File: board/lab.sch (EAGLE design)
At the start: 7 parts

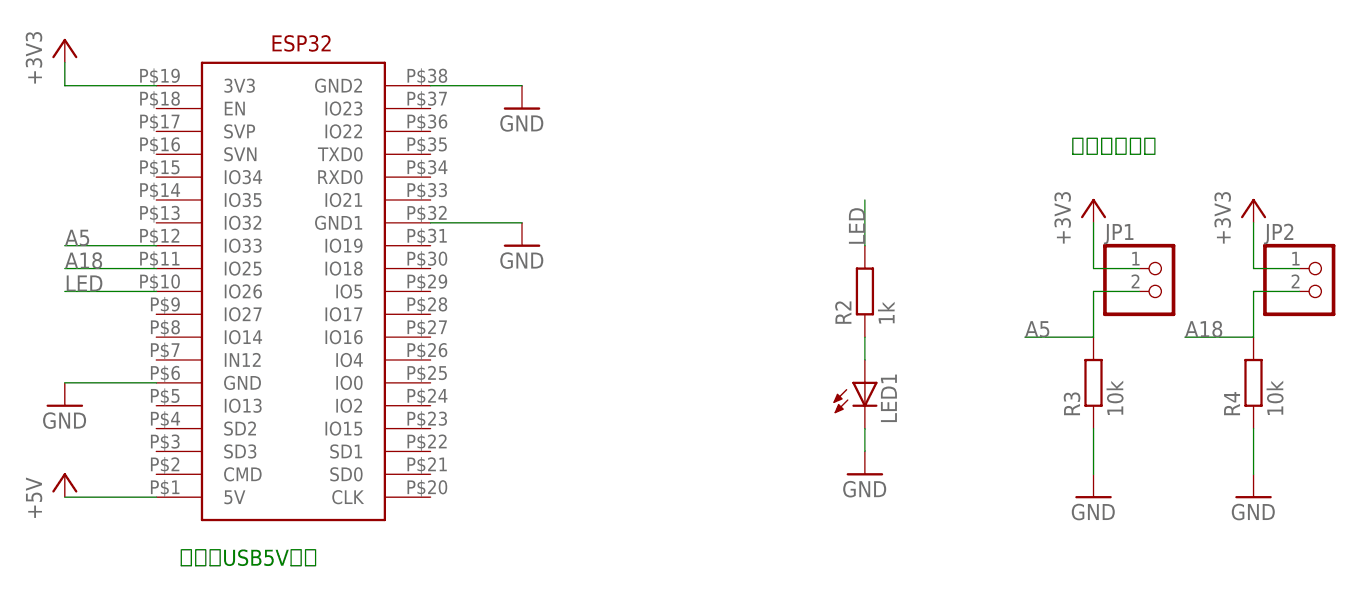
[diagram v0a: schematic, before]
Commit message: add user_button
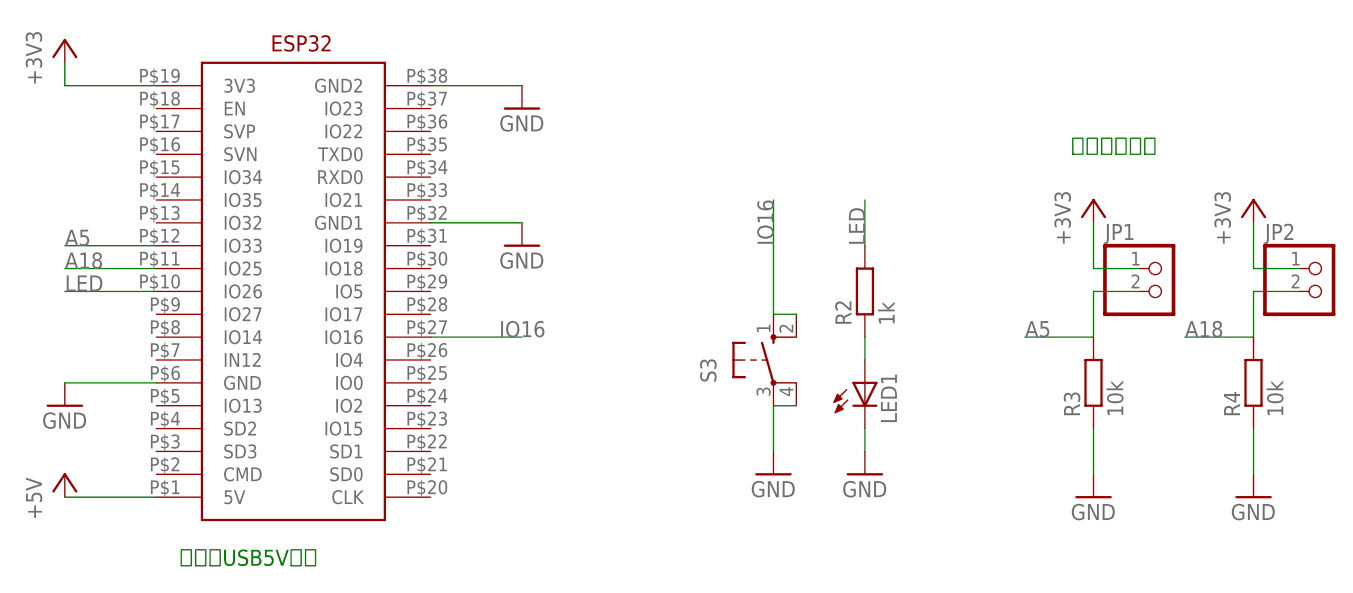
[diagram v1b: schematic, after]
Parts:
- added S3: (no value), switch-omron:10-XX
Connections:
- new net IO16: S3.S, S3.S1, U$1.IO16
- net GND: now also S3.P, S3.P1
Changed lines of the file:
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@@
 <part name="JP1" library="pinhead" deviceset="PINHD-1X2" device=""/>
 <part name="JP2" library="pinhead" deviceset="PINHD-1X2" device=""/>
+<part name="S3" library="switch-omron" deviceset="10-XX" device=""/>
+<part name="GND14" library="supply1" deviceset="GND" device=""/>
 </parts>
 <sheets>
@@
 <instance part="JP1" gate="G$1" x="109.22" y="30.48"/>
 <instance part="JP2" gate="G$1" x="127" y="30.48"/>
+<instance part="S3" gate="1" x="66.04" y="22.86"/>
+<instance part="GND14" gate="1" x="66.04" y="10.16"/>
 </instances>
 <busses>
@@
 <pinref part="R3" gate="G$1" pin="1"/>
 <wire x1="101.6" y1="15.24" x2="101.6" y2="10.16" width="0.1524" layer="91"/>
+</segment>
+<segment>
+<pinref part="S3" gate="1" pin="P"/>
+<wire x1="66.04" y1="17.78" x2="66.04" y2="12.7" width="0.1524" layer="91"/>
+<pinref part="GND14" gate="1" pin="GND"/>
+<pinref part="S3" gate="1" pin="P1"/>
+<wire x1="66.04" y1="17.78" x2="68.58" y2="17.78" width="0.1524" layer="91"/>
 </segment>
 </net>
@@
 </segment>
 </net>
+<net name="IO16" class="0">
+<segment>
+<pinref part="S3" gate="1" pin="S"/>
+<wire x1="66.04" y1="27.94" x2="66.04" y2="40.64" width="0.1524" layer="91"/>
+<label x="66.04" y="35.56" size="1.778" layer="95" rot="R90"/>
+<pinref part="S3" gate="1" pin="S1"/>
+<wire x1="66.04" y1="27.94" x2="68.58" y2="27.94" width="0.1524" layer="91"/>
+</segment>
+<segment>
+<pinref part="U$1" gate="G$1" pin="IO16"/>
+<wire x1="27.94" y1="25.4" x2="38.1" y2="25.4" width="0.1524" layer="91"/>
+<label x="35.56" y="25.4" size="1.778" layer="95"/>
+</segment>
+</net>

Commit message: change ADCpin A18 -> A4
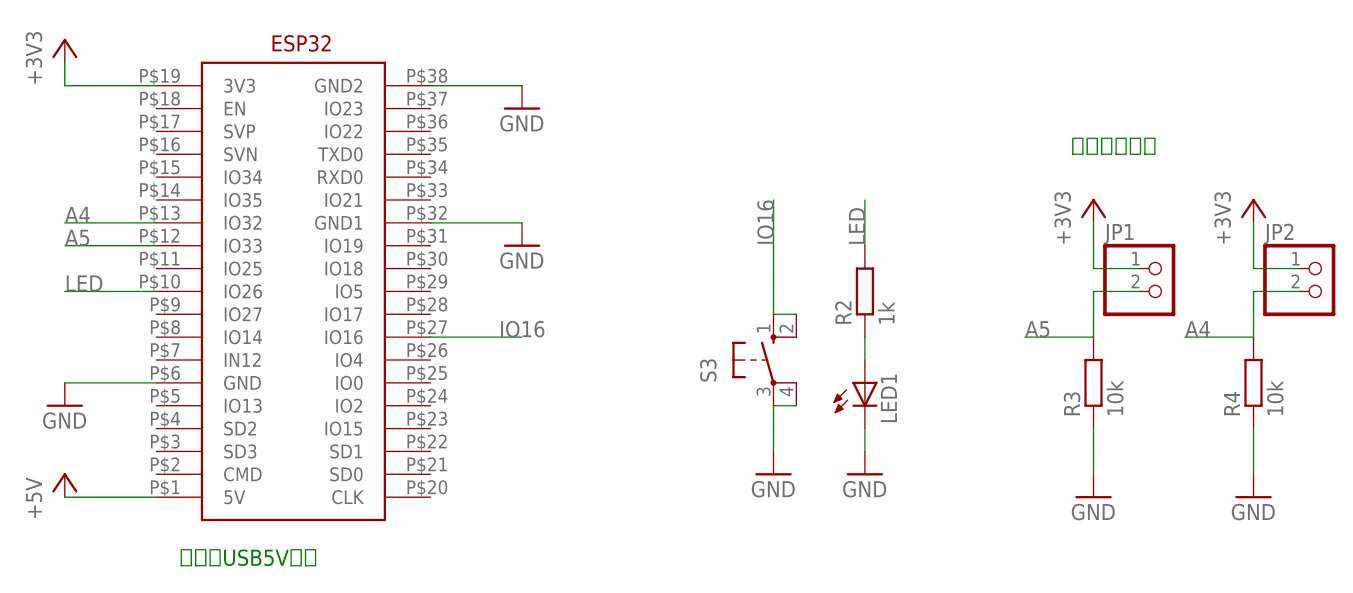
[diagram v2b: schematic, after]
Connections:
- removed net A18: JP2.2, R4.2, U$1.IO25
- new net A4: JP2.2, R4.2, U$1.IO32
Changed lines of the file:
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@@
-</segment>
-</net>
-<net name="A18" class="0">
-<segment>
-<pinref part="U$1" gate="G$1" pin="IO25"/>
-<wire x1="-2.54" y1="33.02" x2="-12.7" y2="33.02" width="0.1524" layer="91"/>
-<label x="-12.7" y="33.02" size="1.778" layer="95"/>
-</segment>
-<segment>
-<pinref part="JP2" gate="G$1" pin="2"/>
-<pinref part="R4" gate="G$1" pin="2"/>
-<wire x1="124.46" y1="30.48" x2="119.38" y2="30.48" width="0.1524" layer="91"/>
-<wire x1="119.38" y1="30.48" x2="119.38" y2="25.4" width="0.1524" layer="91"/>
-<wire x1="119.38" y1="25.4" x2="111.76" y2="25.4" width="0.1524" layer="91"/>
-<label x="111.76" y="25.4" size="1.778" layer="95"/>
 </segment>
 </net>
@@
 </segment>
 </net>
+<net name="A4" class="0">
+<segment>
+<pinref part="U$1" gate="G$1" pin="IO32"/>
+<wire x1="-2.54" y1="38.1" x2="-12.7" y2="38.1" width="0.1524" layer="91"/>
+<label x="-12.7" y="38.1" size="1.778" layer="95"/>
+</segment>
+<segment>
+<pinref part="JP2" gate="G$1" pin="2"/>
+<pinref part="R4" gate="G$1" pin="2"/>
+<wire x1="124.46" y1="30.48" x2="119.38" y2="30.48" width="0.1524" layer="91"/>
+<wire x1="119.38" y1="30.48" x2="119.38" y2="25.4" width="0.1524" layer="91"/>
+<wire x1="119.38" y1="25.4" x2="111.76" y2="25.4" width="0.1524" layer="91"/>
+<label x="111.76" y="25.4" size="1.778" layer="95"/>
+</segment>
+</net>
